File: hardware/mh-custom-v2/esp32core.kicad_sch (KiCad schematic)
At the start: 1 part

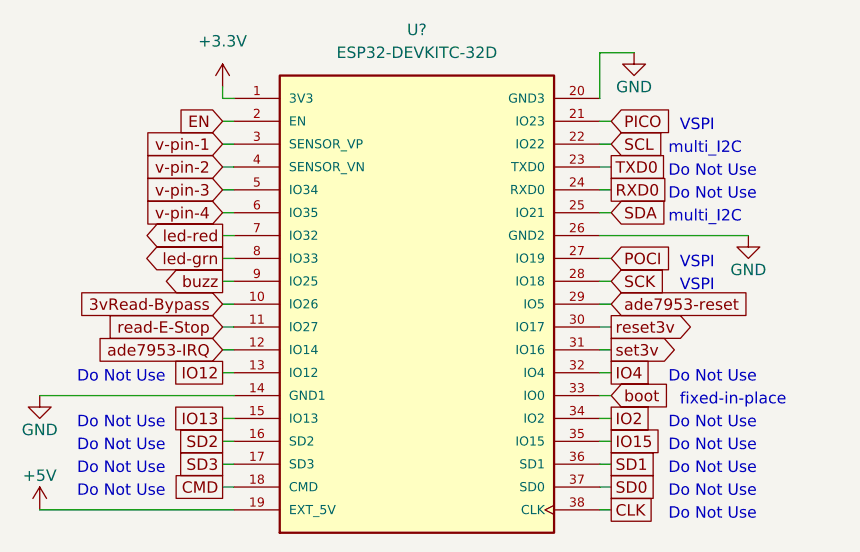
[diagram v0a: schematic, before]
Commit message: low-voltage side of V2 board rebuilt. Started on high-voltage side
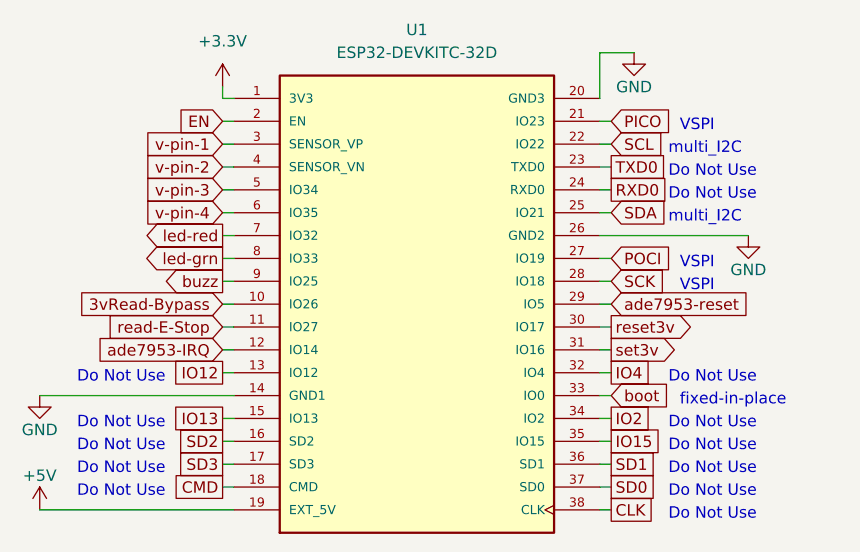
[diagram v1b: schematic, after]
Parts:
- gave numbers to parts that had none: 1
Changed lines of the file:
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@@
   (symbol (lib_id "power:GND") (at 104.14 91.44 0) (unit 1)
     (in_bom yes) (on_board yes)
-    (property "Reference" "#PWR?" (id 0) (at 104.14 97.79 0)
+    (property "Reference" "#PWR0103" (id 0) (at 104.14 97.79 0)
       (effects (font (size 1.27 1.27)) hide)
     )
@@
   (symbol (lib_id "power:GND") (at 182.88 73.66 0) (unit 1)
     (in_bom yes) (on_board yes)
-    (property "Reference" "#PWR?" (id 0) (at 182.88 80.01 0)
+    (property "Reference" "#PWR0102" (id 0) (at 182.88 80.01 0)
       (effects (font (size 1.27 1.27)) hide)
     )
@@
   (symbol (lib_id "power:+5V") (at 104.14 104.14 0) (unit 1)
     (in_bom yes) (on_board yes)
-    (property "Reference" "#PWR?" (id 0) (at 104.14 107.95 0)
+    (property "Reference" "#PWR0104" (id 0) (at 104.14 107.95 0)
       (effects (font (size 1.27 1.27)) hide)
     )
@@
   (symbol (lib_id "esp32-devkitc-v4:ESP32-DEVKITC-32D") (at 146.05 81.28 0) (unit 1)
     (in_bom no) (on_board no) (fields_autoplaced)
-    (property "Reference" "U?" (id 0) (at 146.05 50.8 0))
+    (property "Reference" "U1" (id 0) (at 146.05 50.8 0))
     (property "Value" "ESP32-DEVKITC-32D" (id 1) (at 146.05 53.34 0))
     (property "Footprint" "esp32-devkitc-v4:MODULE_ESP32-DEVKITC-32D" (id 2) (at 146.05 81.28 0)
@@
   (symbol (lib_id "power:GND") (at 170.18 53.34 0) (unit 1)
     (in_bom yes) (on_board yes)
-    (property "Reference" "#PWR?" (id 0) (at 170.18 59.69 0)
+    (property "Reference" "#PWR0101" (id 0) (at 170.18 59.69 0)
       (effects (font (size 1.27 1.27)) hide)
     )
@@
   (symbol (lib_id "power:+3.3V") (at 124.46 57.15 0) (unit 1)
     (in_bom yes) (on_board yes) (fields_autoplaced)
-    (property "Reference" "#PWR?" (id 0) (at 124.46 60.96 0)
+    (property "Reference" "#PWR0105" (id 0) (at 124.46 60.96 0)
       (effects (font (size 1.27 1.27)) hide)
     )
